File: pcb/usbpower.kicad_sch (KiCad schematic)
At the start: 13 parts, among them J1 USB_C_Receptacle_USB2.0_16P, Q1 AO3401A, U1 SPX3819M5-L-3-3

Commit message: with errors
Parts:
- added U5: USBLC6-2P6, Package_TO_SOT_SMD:SOT-666, symbol Power_Protection:USBLC6-2P6
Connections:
- net GND: now also U5.2 (GND)
- net D+: no longer names the net of J1.A6 (D+), J1.B6 (D+)
- net D+: now also U5.3 (I/O2)
- net D-: no longer names the net of J1.A7 (D-), J1.B7 (D-)
- net D-: now also U5.1 (I/O1)
- new net USBD+: U5.6 (I/O1)
- new net USBD-: U5.4 (I/O2)
- no-connect marks 2 -> 3
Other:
- moved on the sheet: C1, C2, C3, C4, D1, D2, Q1, R1, R2, R3, R4, U1

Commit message: schematic done
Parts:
- C1, C2, C3, C4: footprint (none) -> Capacitor_SMD:C_0603_1608Metric
- D2: footprint (none) -> LED_SMD:LED_0603_1608Metric
- J1: footprint (none) -> Connector_USB:USB_C_Receptacle_GCT_USB4085
- R1, R2, R3, R4: footprint (none) -> Resistor_SMD:R_0603_1608Metric
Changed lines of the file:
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@@
 			)
 		)
-		(property "Footprint" ""
+		(property "Footprint" "Resistor_SMD:R_0603_1608Metric"
 			(at 146.812 104.14 90)
 			(effects
@@
 			)
 		)
-		(property "Footprint" ""
+		(property "Footprint" "Resistor_SMD:R_0603_1608Metric"
 			(at 150.622 87.63 90)
 			(effects
@@
 			)
 		)
-		(property "Footprint" ""
+		(property "Footprint" "Resistor_SMD:R_0603_1608Metric"
 			(at 144.272 104.14 90)
 			(effects
@@
 			)
 		)
-		(property "Footprint" ""
+		(property "Footprint" "Resistor_SMD:R_0603_1608Metric"
 			(at 236.982 86.36 90)
 			(effects
@@
 			)
 		)
-		(property "Footprint" ""
+		(property "Footprint" "Connector_USB:USB_C_Receptacle_GCT_USB4085"
 			(at 102.87 97.79 0)
 			(effects
@@
 			)
 		)
-		(property "Footprint" ""
+		(property "Footprint" "LED_SMD:LED_0603_1608Metric"
 			(at 238.76 96.52 0)
 			(effects
@@
 			)
 		)
-		(property "Footprint" ""
+		(property "Footprint" "Capacitor_SMD:C_0603_1608Metric"
 			(at 230.8352 90.17 0)
 			(effects
@@
 			)
 		)
-		(property "Footprint" ""
+		(property "Footprint" "Capacitor_SMD:C_0603_1608Metric"
 			(at 172.4152 91.44 0)
 			(effects
@@
 			)
 		)
-		(property "Footprint" ""
+		(property "Footprint" "Capacitor_SMD:C_0603_1608Metric"
 			(at 210.5152 93.98 0)
 			(effects
@@
 			)
 		)
-		(property "Footprint" ""
+		(property "Footprint" "Capacitor_SMD:C_0603_1608Metric"
 			(at 221.9452 90.17 0)
 			(effects

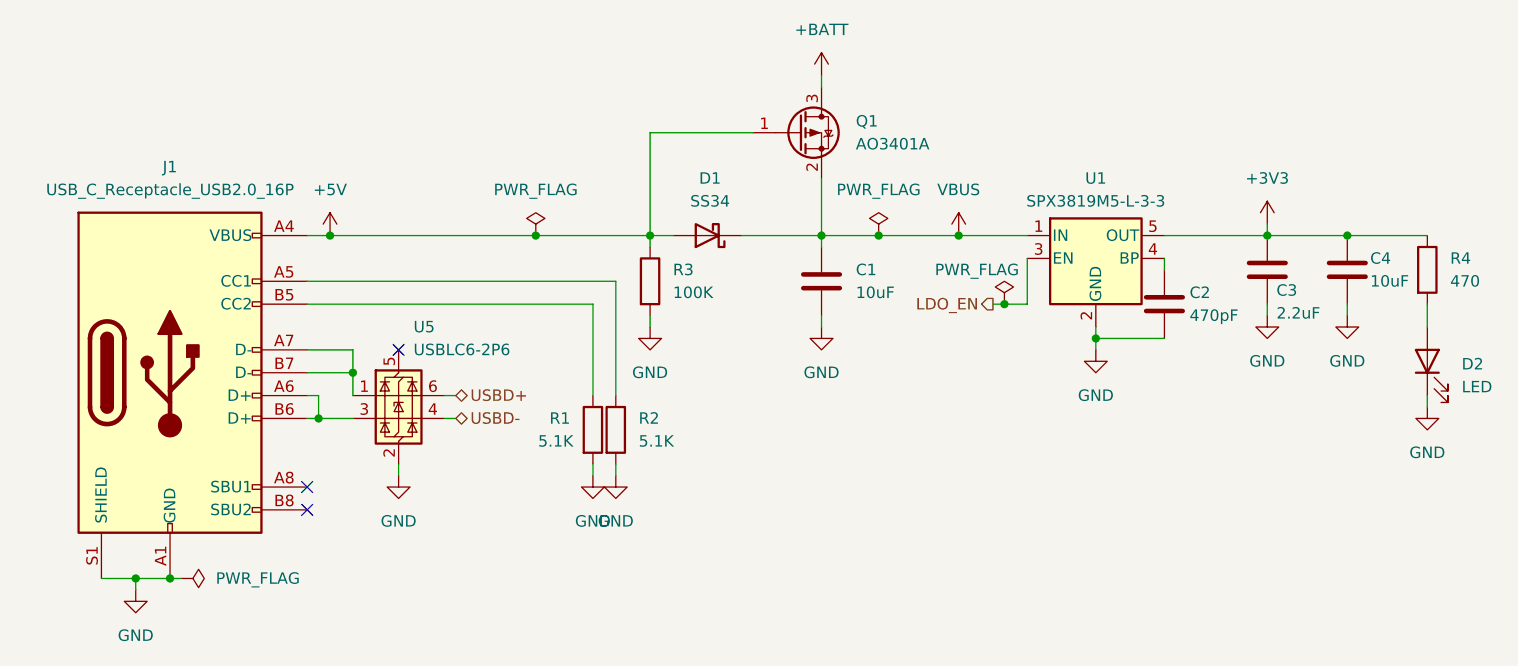
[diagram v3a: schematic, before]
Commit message: without gnd
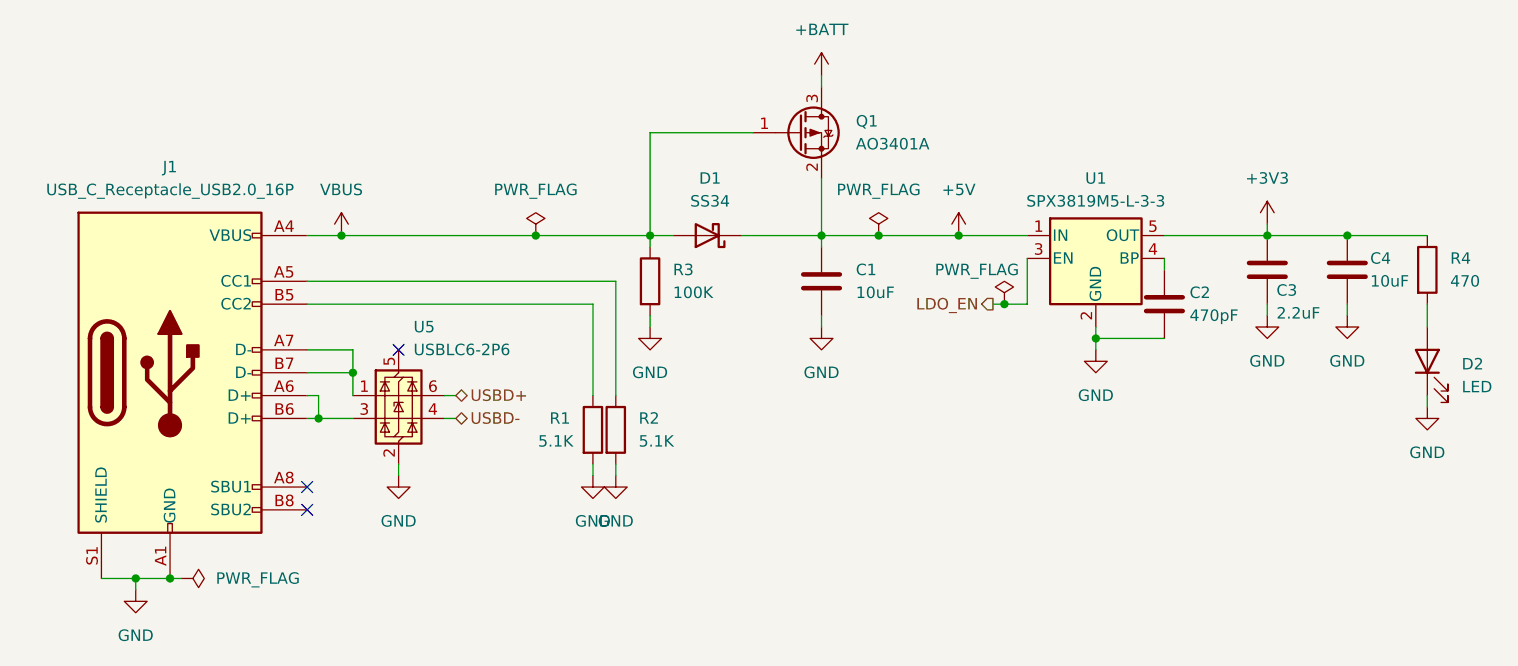
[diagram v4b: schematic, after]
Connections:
- net +5V: now also C1.1, D1.1 (K), Q1.2 (S), U1.1 (IN); no longer D1.2 (A), J1.A4 (VBUS), J1.A9 (VBUS), J1.B4 (VBUS), J1.B9 (VBUS), Q1.1 (G), R3.1
- net VBUS: now also D1.2 (A), J1.A4 (VBUS), J1.A9 (VBUS), J1.B4 (VBUS), J1.B9 (VBUS), Q1.1 (G), R3.1; no longer C1.1, D1.1 (K), Q1.2 (S), U1.1 (IN)
